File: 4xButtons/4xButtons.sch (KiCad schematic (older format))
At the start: 12 parts, among them J1 Conn_01x01_Male, J2 Conn_01x01_Male, J3 Conn_01x01_Male, J4 Conn_01x01_Male, J5 Conn_01x01_Male, J6 Conn_01x01_Male, J7 Conn_01x01_Male, J8 Conn_01x01_Male, SW1 SW_Push, SW2 SW_Push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

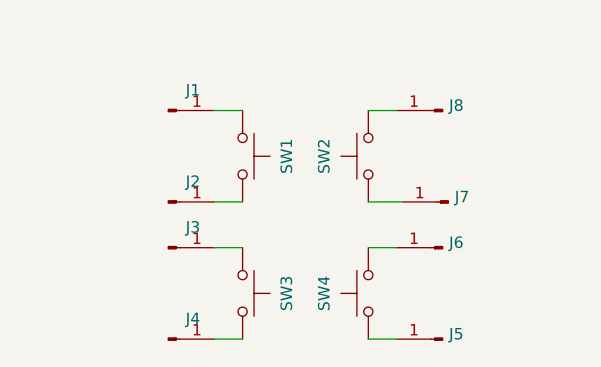
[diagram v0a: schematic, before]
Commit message: Change sheet size to 8.5x11
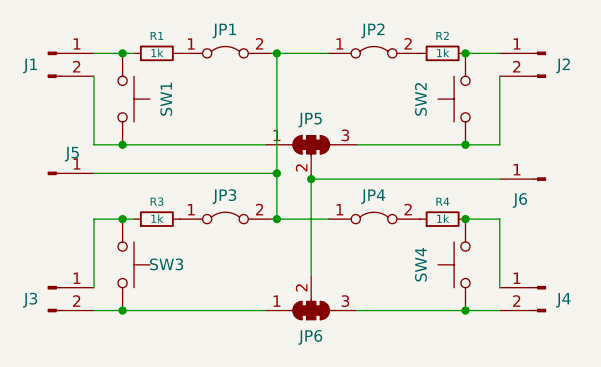
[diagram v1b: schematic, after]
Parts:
- removed J1, J2, J3, J4, J7, J8: Conn_01x01_Male, Connector_PinHeader_2.54mm:PinHeader_1x01_P2.54mm_Vertical, symbol Connector:Conn_01x01_Male
- added J1, J2, J3, J4: Conn_01x02_Male, Connector_PinHeader_2.54mm:PinHeader_1x02_P2.54mm_Vertical, symbol Connector:Conn_01x02_Male
- added JP1, JP2, JP3, JP4: Jumper_2_Bridged, Jumper:SolderJumper-2_P1.3mm_Bridged_Pad1.0x1.5mm, symbol Jumper:Jumper_2_Bridged
- added JP5, JP6: SolderJumper_3_Bridged123, BreakoutBoards:SolderJumper-3_P1.3mm_Bridged12_Pad1.0x1.5mm_NumberLabels, symbol Jumper:SolderJumper_3_Bridged123
- added R1, R2, R3, R4: 1k, Resistor_SMD:R_0603_1608Metric, symbol Device:R_Small
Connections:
- net at SW1.1: now also J1.1 (Pin_1), R1.1
- net at SW1.2: now also J1.2 (Pin_2), JP5.1 (A)
- net at SW2.2: now also J2.1 (Pin_1), R2.2
- net at SW2.1: now also J2.2 (Pin_2), JP5.3 (B)
- net at SW4.2: now also J4.1 (Pin_1), R4.2; no longer J6.1 (Pin_1)
- net at SW3.1: now also J3.1 (Pin_1), R3.1
- net at SW3.2: now also J3.2 (Pin_2), JP6.1 (A)
- net at SW4.1: now also J4.2 (Pin_2), JP6.3 (B); no longer J5.1 (Pin_1)
- new net: JP1.1 (A), R1.2
- new net: JP2.2 (B), R2.1
- new net: JP4.2 (B), R4.1
- new net: JP3.1 (A), R3.2
- new net: J5.1 (Pin_1), JP1.2 (B), JP2.1 (A), JP3.2 (B), JP4.1 (A)
- new net: J6.1 (Pin_1), JP5.2 (C), JP6.2 (C)
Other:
- moved on the sheet: SW1, SW2, SW3, SW4
